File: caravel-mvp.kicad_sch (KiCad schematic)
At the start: 47 parts, among them J2 Conn_01x02, J3 Conn_02x04_Odd_Even, J4 Conn_01x06, J6 Conn_02x18_Odd_Even, J6 USB_C_Receptacle_USB2.0, J9 613012243121, SW3 B3U-1000P, U1 Caravel_QFN_TT3, U1 W25Q32JVSS, X1 10MHz

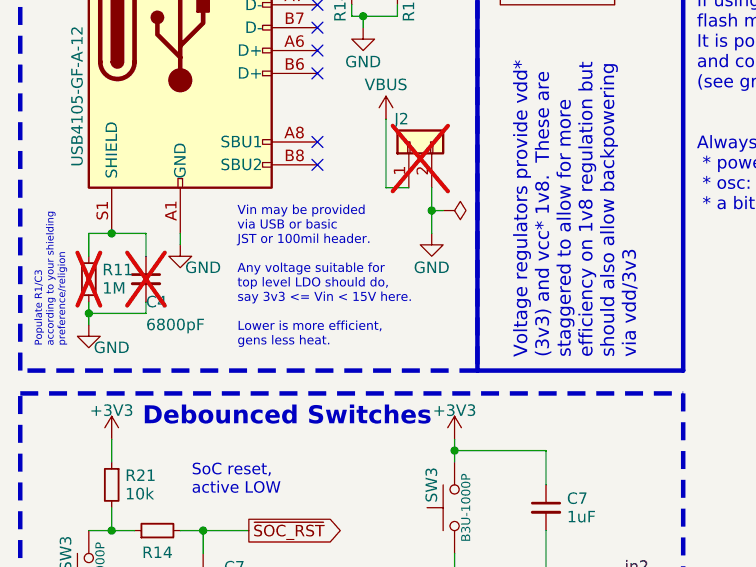
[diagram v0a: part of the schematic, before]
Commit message: warning for max V on LDO
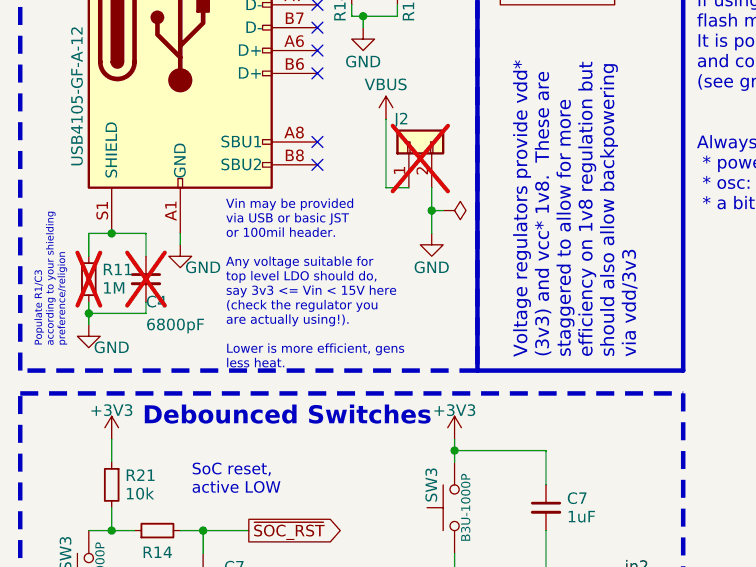
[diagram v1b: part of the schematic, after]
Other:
- note added: "Vin may be provided via USB or basic JST or 100mil header. Any voltage suitable for top level LDO should do, say 3v3 <= Vin < 15V here (check the regulator you are actually using!). Lower is more efficient, gens less heat."
- note removed: "Vin may be provided via USB or basic JST or 100mil header. Any voltage suitable for top level LDO should do, say 3v3 <= Vin < 15V here. Lower is more efficient, gens less heat."
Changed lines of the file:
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@@
     (effects (font (size 1.6 1.6) (thickness 0.254) bold) (justify left bottom))
   )
-  (text "Vin may be provided\nvia USB or basic \nJST or 100mil header.\n\nAny voltage suitable for \ntop level LDO should do,\nsay 3v3 <= Vin < 15V here.\n\nLower is more efficient,\ngens less heat."
-    (at 36.83 73.66 0)
+  (text "Vin may be provided\nvia USB or basic JST \nor 100mil header.\n\nAny voltage suitable for \ntop level LDO should do,\nsay 3v3 <= Vin < 15V here\n(check the regulator you\nare actually using!).\n\nLower is more efficient, gens \nless heat."
+    (at 35.56 76.2 0)
     (effects (font (size 1 1)) (justify left bottom))
   )
